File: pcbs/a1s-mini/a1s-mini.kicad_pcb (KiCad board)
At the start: 2 copper layers, 58.8 x 55.7 mm, 85 parts, among them J1 UART1, J2 SJ-3524-SMT-TR-PI, J3 Audio Out, J4 UART0, J5 USB4105-GF-A, J6 USB4105-GF-A, Q3 BC818, Q4 MBT3904DW1, Q6 MBT3904DW1, U1 ESP32 A1S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

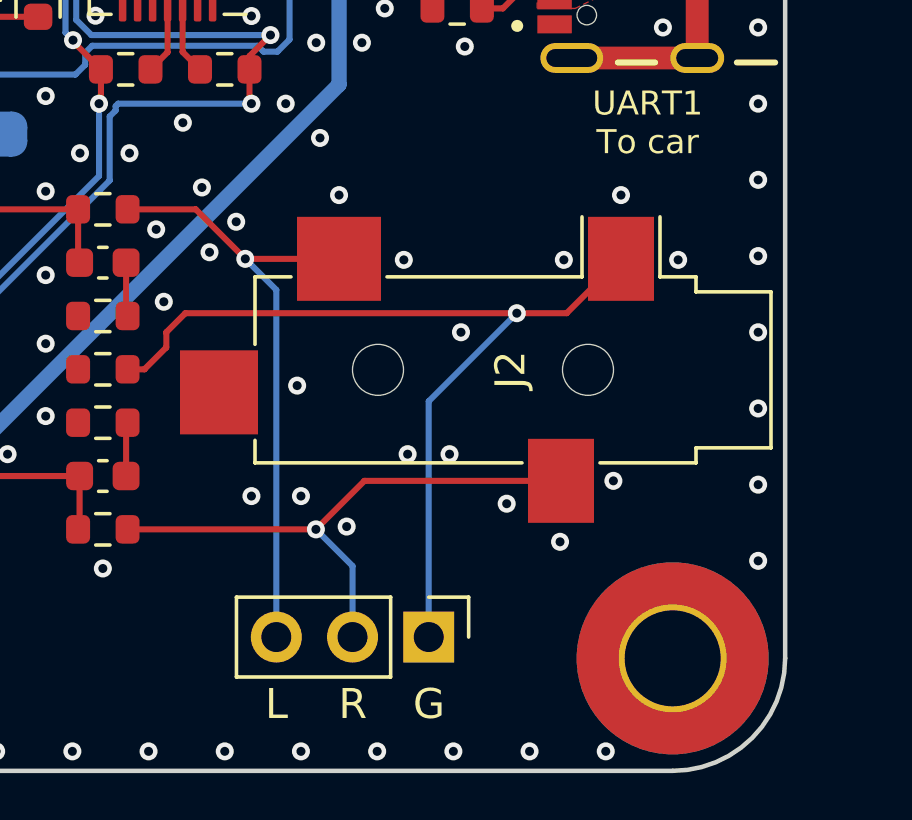
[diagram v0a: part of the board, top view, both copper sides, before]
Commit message: Moving audio jack and generating step files
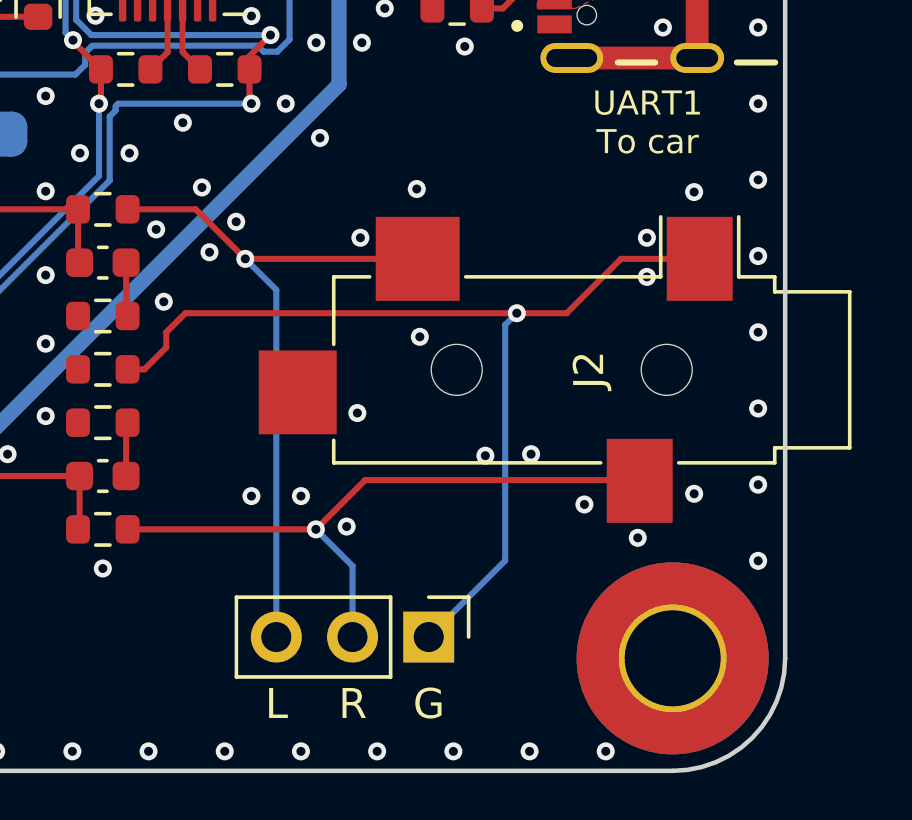
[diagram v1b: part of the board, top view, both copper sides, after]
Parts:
- moved J2 2.62 mm to (179.4, 122.8)
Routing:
- net ROUT: track 19.2 -> 21.9 mm
- net LOUT: track 20.8 -> 23.4 mm
- net AGND: track 30.3 -> 32.9 mm
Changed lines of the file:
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@@
 	(title_block
 		(title "A1S Mini Board")
-		(date "2025-03-30")
-		(rev "0.3.0")
+		(date "2025-05-25")
+		(rev "0.3.1")
 		(company "Martin Roger")
 	)
@@
 		(tags "Switch")
 		(property "Reference" "S2"
-			(at -0.85 0 270)
+			(at -0.85 0 90)
 			(layer "F.SilkS")
 			(effects
@@
 		)
 		(property "Value" "TL3305BF260QG"
-			(at -0.85 0 270)
+			(at -0.85 0 90)
 			(layer "F.SilkS")
 			(hide yes)
@@
 		)
 		(property "Datasheet" "https://configured-product-images.s3.amazonaws.com/2D/specs/TL3305BF260QG.pdf"
-			(at 0 0 270)
+			(at 0 0 90)
 			(layer "F.Fab")
 			(hide yes)
@@
 		)
 		(property "Description" "TACT, 50mA, 12VDC SPST-NO, Off-(On) Surface Mount"
-			(at 0 0 270)
+			(at 0 0 90)
 			(layer "F.Fab")
 			(hide yes)
@@
 		)
 		(embedded_fonts no)
+		(model "${PRIVATE_3DMODELS}/TL3305BF260QG.stp"
+			(offset
+				(xyz 0 0 0)
+			)
+			(scale
+				(xyz 1 1 1)
+			)
+			(rotate
+				(xyz 0 0 0)
+			)
+		)
 	)
 	(footprint "Capacitor_SMD:C_0805_2012Metric"
@@
 	(footprint "Connector_Audio:Jack_3.5mm_CUI_SJ-3524-SMT_Horizontal"
 		(layer "F.Cu")
-		(at 176.74 122.792 -90)
+		(at 179.364 122.792 -90)
 		(descr "3.5 mm, Stereo, Right Angle, Surface Mount (SMT), Audio Jack Connector (https://www.cui.com/product/resource/sj-352x-smt-series.pdf)")
 		(tags "3.5mm audio cui horizontal jack stereo")
@@
 		)
 		(embedded_fonts no)
-		(model "${KICAD6_3DMODEL_DIR}/Connector_Audio.3dshapes/Jack_3.5mm_CUI_SJ-3524-SMT_Horizontal.wrl"
+		(model "${PRIVATE_3DMODELS}/SJ-3524-SMT-TR-PI.stp"
 			(offset
-				(xyz 0 0 0)
+				(xyz 0 6 2.5)
 			)
 			(scale
@@
 			)
 			(rotate
-				(xyz 0 0 0)
+				(xyz 90 180 -0)
 			)
 		)
@@
 		(tags "Switch")
 		(property "Reference" "S1"
-			(at -0.85 0 270)
+			(at -0.85 0 90)
 			(layer "F.SilkS")
 			(effects
@@
 		)
 		(property "Value" "TL3305BF260QG"
-			(at -0.85 0 270)
+			(at -0.85 0 90)
 			(layer "F.SilkS")
 			(hide yes)
@@
 		)
 		(property "Datasheet" "https://configured-product-images.s3.amazonaws.com/2D/specs/TL3305BF260QG.pdf"
-			(at 0 0 270)
+			(at 0 0 90)
 			(layer "F.Fab")
 			(hide yes)
@@
 		)
 		(property "Description" "TACT, 50mA, 12VDC SPST-NO, Off-(On) Surface Mount"
-			(at 0 0 270)
+			(at 0 0 90)
 			(layer "F.Fab")
 			(hide yes)
@@
 		)
 		(embedded_fonts no)
+		(model "${PRIVATE_3DMODELS}/TL3305BF260QG.stp"
+			(offset
+				(xyz 0 0 0)
+			)
+			(scale
+				(xyz 1 1 1)
+			)
+			(rotate
+				(xyz 0 0 0)
+			)
+		)
 	)
 	(footprint "Resistor_SMD:R_0603_1608Metric"
@@
 	)
 	(via
-		(at 173.228 125.603)
+		(at 175.8188 125.6538)
 		(size 0.6)
 		(drill 0.3)
@@
 	)
 	(via
-		(at 182.245 119.126)
+		(at 182.7784 116.8654)
 		(size 0.6)
 		(drill 0.3)
@@
 	)
 	(via
-		(at 169.545 123.317)
+		(at 171.5516 124.2314)
 		(size 0.6)
 		(drill 0.3)
@@
 	)
 	(via
-		(at 178.308 128.524)
+		(at 180.8988 128.392002)
 		(size 0.6)
 		(drill 0.3)
@@
 	)
 	(via
-		(at 176.53 127.254)
+		(at 179.1208 127.2794)
 		(size 0.6)
 		(drill 0.3)
@@
 	)
 	(via
-		(at 180.34 116.967)
+		(at 181.2036 119.6936)
 		(size 0.6)
 		(drill 0.3)
@@
 	)
 	(via
-		(at 180.086 126.492)
+		(at 182.7784 126.9238)
 		(size 0.6)
 		(drill 0.3)
@@
 	)
 	(via
-		(at 170.942 116.967)
+		(at 171.6532 118.3894)
 		(size 0.6)
 		(drill 0.3)
@@
 	)
 	(via
-		(at 174.625 125.603)
+		(at 177.3428 125.603)
 		(size 0.6)
 		(drill 0.3)
@@
 	)
 	(via
-		(at 175.006 121.539)
+		(at 173.6344 121.6914)
 		(size 0.6)
 		(drill 0.3)
@@
 	)
 	(via
-		(at 178.435 119.126)
+		(at 181.2036 118.3894)
 		(size 0.6)
 		(drill 0.3)
@@
 	)
 	(via
-		(at 173.101 119.126)
+		(at 173.5328 116.7638)
 		(size 0.6)
 		(drill 0.3)
@@
 	)
 	(segment
-		(start 171.787 126.492)
-		(end 178.34 126.492)
+		(start 170.17 128.109)
+		(end 171.8124 126.4666)
 		(width 0.2032)
 		(layer "F.Cu")
@@
 	)
 	(segment
-		(start 170.17 128.109)
-		(end 171.787 126.492)
+		(start 180.9386 126.4666)
+		(end 180.964 126.492)
+		(width 0.2032)
+		(layer "F.Cu")
+		(net 33)
+	)
+	(segment
+		(start 171.8124 126.4666)
+		(end 180.9386 126.4666)
 		(width 0.2032)
 		(layer "F.Cu")
@@
 	)
 	(segment
-		(start 178.528 120.904)
-		(end 180.34 119.092)
+		(start 163.893 122.775)
+		(end 164.455 122.775)
 		(width 0.2032)
 		(layer "F.Cu")
@@
 	)
 	(segment
-		(start 163.893 122.775)
-		(end 164.455 122.775)
+		(start 180.34 119.092)
+		(end 182.964 119.092)
 		(width 0.2032)
 		(layer "F.Cu")
@@
 		(net 34)
 	)
+	(segment
+		(start 178.528 120.904)
+		(end 180.34 119.092)
+		(width 0.2032)
+		(layer "F.Cu")
+		(net 34)
+	)
 	(via
 		(at 176.867 120.904)
@@
 	)
 	(segment
-		(start 173.931 123.84)
+		(start 176.4792 121.2918)
 		(end 176.867 120.904)
 		(width 0.2032)
@@
 	(segment
 		(start 173.931 131.699)
-		(end 173.931 123.84)
+		(end 176.4792 129.1508)
+		(width 0.2032)
+		(layer "B.Cu")
+		(net 34)
+	)
+	(segment
+		(start 176.4792 129.1508)
+		(end 176.4792 121.2918)
 		(width 0.2032)
 		(layer "B.Cu")
@@
 	)
 	(segment
-		(start 167.816 119.092)
-		(end 170.94 119.092)
+		(start 163.893 117.441)
+		(end 166.165 117.441)
 		(width 0.2032)
 		(layer "F.Cu")
@@
 	)
 	(segment
-		(start 163.893 117.441)
-		(end 166.165 117.441)
+		(start 167.816 119.092)
+		(end 173.564 119.092)
 		(width 0.2032)
 		(layer "F.Cu")
@@
 	(group ""
 		(members "010ed563-2973-4e7b-880b-ac3cfb64729f" "01276b8d-2b07-49d3-8b35-fdecf44a092f"
-			"019a97af-5de7-4efe-972a-8204659258c9" "0bc8b6e9-098f-455f-a2b6-f17a9d852d70"
-			"0be3b034-8138-41b2-8697-4d37a17a84a4" "1277cde9-51e9-4f09-85db-96225ab56807"
+			"0bc8b6e9-098f-455f-a2b6-f17a9d852d70" "0be3b034-8138-41b2-8697-4d37a17a84a4"
+			"1277cde9-51e9-4f09-85db-96225ab56807" "16802a33-bfa3-482c-9e4f-84b36f7dd177"
 			"1f55c12f-7500-44a8-9a40-de71dd5c2e10" "2320cddf-c750-480e-808d-3dbd92fe251d"
 			"2635c3ab-f4d5-4ea3-8317-cc488b28a56d" "27dbc821-cc4b-4ea6-ad66-3b0d750dda18"
 			"2ce1c9cf-3d4a-4b50-9b31-e205f036385f" "304ad4f1-862e-4027-8de5-301e5c9bb41e"
-			"3283374a-ec22-4d03-80e8-8ad2329dba5f" "355cc9c1-65e6-4e68-a974-cbbdd1257902"
-			"35b4e900-2bed-4ea8-b7e7-b8250b1e7e7e" "3bdbe9e9-9197-4c0e-a543-8e46b804b0dc"
-			"4782a773-90a6-4148-b0a7-9dd6eefd5aad" "4c52461a-149b-4eec-a428-97cf9bf35de8"
-			"5c99fa24-4401-4d5a-997f-6d78716bc5f5" "5d014071-d2dc-4647-beaf-cba16b22cd9f"
-			"8ee44f09-00b1-4cb8-a334-ebd31d421489" "9464d84d-46a6-4a53-afc5-3f068152bc37"
-			"b62076f0-405c-4baa-b1f5-f8bcf2d20abd" "b8b7875e-48a3-4bdb-b0db-3715a3c873ef"
-			"bbbde7ee-d092-4d43-b47f-1ea3ba58ced9" "bce551e3-f423-4053-9973-22389445b177"
-			"c368fc1b-c9c4-44e1-99a4-be5dbafa2c78" "c8101ae0-b9df-476c-a6fa-1832a03521fa"
-			"cd4b371d-78d5-4685-ade5-c527481dbb93" "cea4292e-6d22-40c0-a3ef-10f58e66caf0"
-			"da937504-e6c3-46ed-a387-d5830cbeae16" "e6eb6426-162a-4115-b2a7-4587bebc7a9c"
-			"ec039ec8-b2e6-4db4-9b6e-e6335db5a8b9" "eef33f5e-9a19-4485-b453-f566f85e2875"
-			"f202a222-b79e-45f9-99d0-3975618f77dc" "f317a6f2-5063-4160-a05b-54ee9751d1aa"
-			"f3bd3b37-f068-4793-a604-252e1f766a4c"
+			"3bdbe9e9-9197-4c0e-a543-8e46b804b0dc" "4782a773-90a6-4148-b0a7-9dd6eefd5aad"
+			"4c52461a-149b-4eec-a428-97cf9bf35de8" "5c99fa24-4401-4d5a-997f-6d78716bc5f5"
+			"5d014071-d2dc-4647-beaf-cba16b22cd9f" "6428761d-30dd-4c5b-ad00-7d5e50292759"
+			"6544f0f1-11bd-4078-b5a1-d2c90a1d2fdb" "6767676a-2073-418f-8eb7-74b574d95305"
+			"85cc0403-8287-4ccc-9240-b6bb848303b7" "8ee44f09-00b1-4cb8-a334-ebd31d421489"
+			"9464d84d-46a6-4a53-afc5-3f068152bc37" "98181832-dbcc-4c7b-bd6b-59713328d394"
+			"a62cc70d-f242-49f9-aa8d-1462106ee1b0" "b62076f0-405c-4baa-b1f5-f8bcf2d20abd"
+			"b78e9ece-bcde-4c88-a0b1-0686802ee165" "b8b7875e-48a3-4bdb-b0db-3715a3c873ef"
+			"bbbde7ee-d092-4d43-b47f-1ea3ba58ced9" "c368fc1b-c9c4-44e1-99a4-be5dbafa2c78"
+			"c8101ae0-b9df-476c-a6fa-1832a03521fa" "cd4b371d-78d5-4685-ade5-c527481dbb93"
+			"cea4292e-6d22-40c0-a3ef-10f58e66caf0" "da937504-e6c3-46ed-a387-d5830cbeae16"
+			"e6eb6426-162a-4115-b2a7-4587bebc7a9c" "ec039ec8-b2e6-4db4-9b6e-e6335db5a8b9"
+			"f2edf953-51db-454e-9f92-fcd6f25702e4" "f317a6f2-5063-4160-a05b-54ee9751d1aa"
+			"f3bd3b37-f068-4793-a604-252e1f766a4c" "f6861546-4d09-4eba-b4d5-1c9548f0ff14"
 		)
 	)

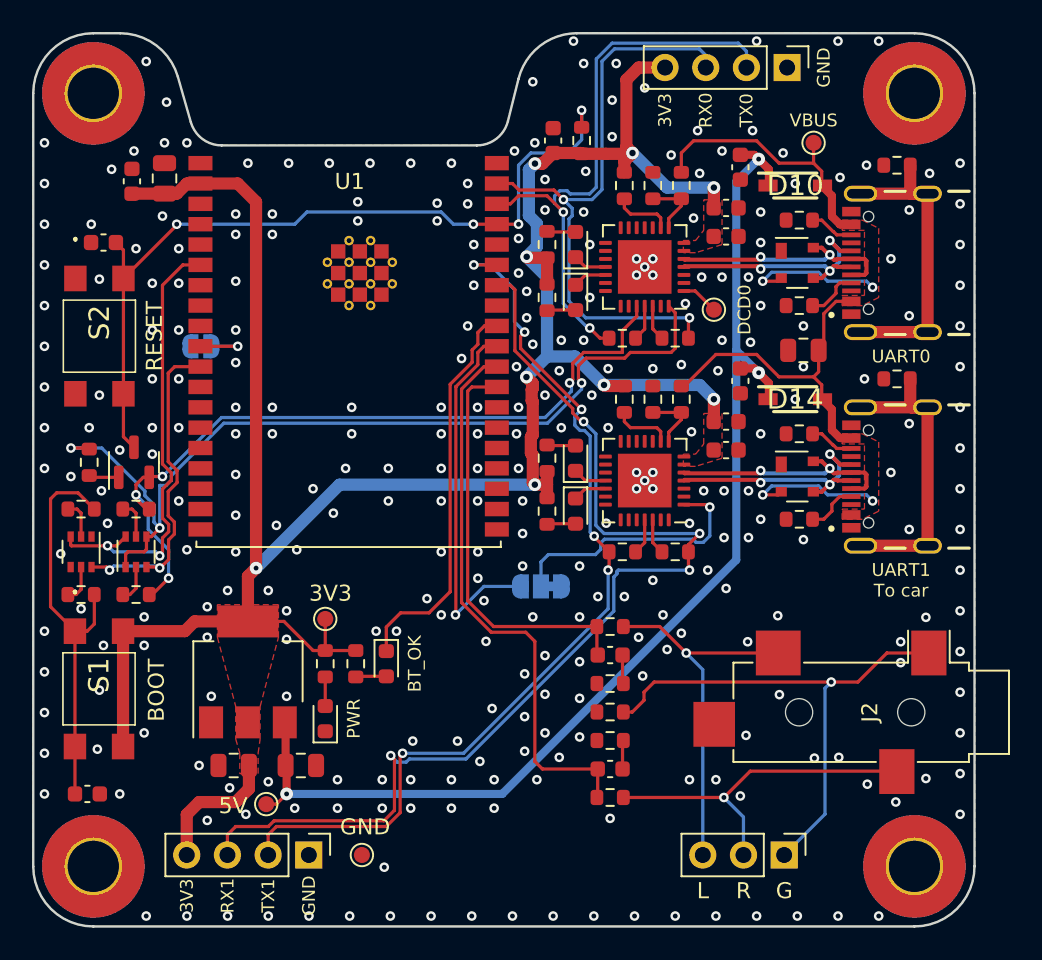
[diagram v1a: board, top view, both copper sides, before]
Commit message: Move to CP2102 non N
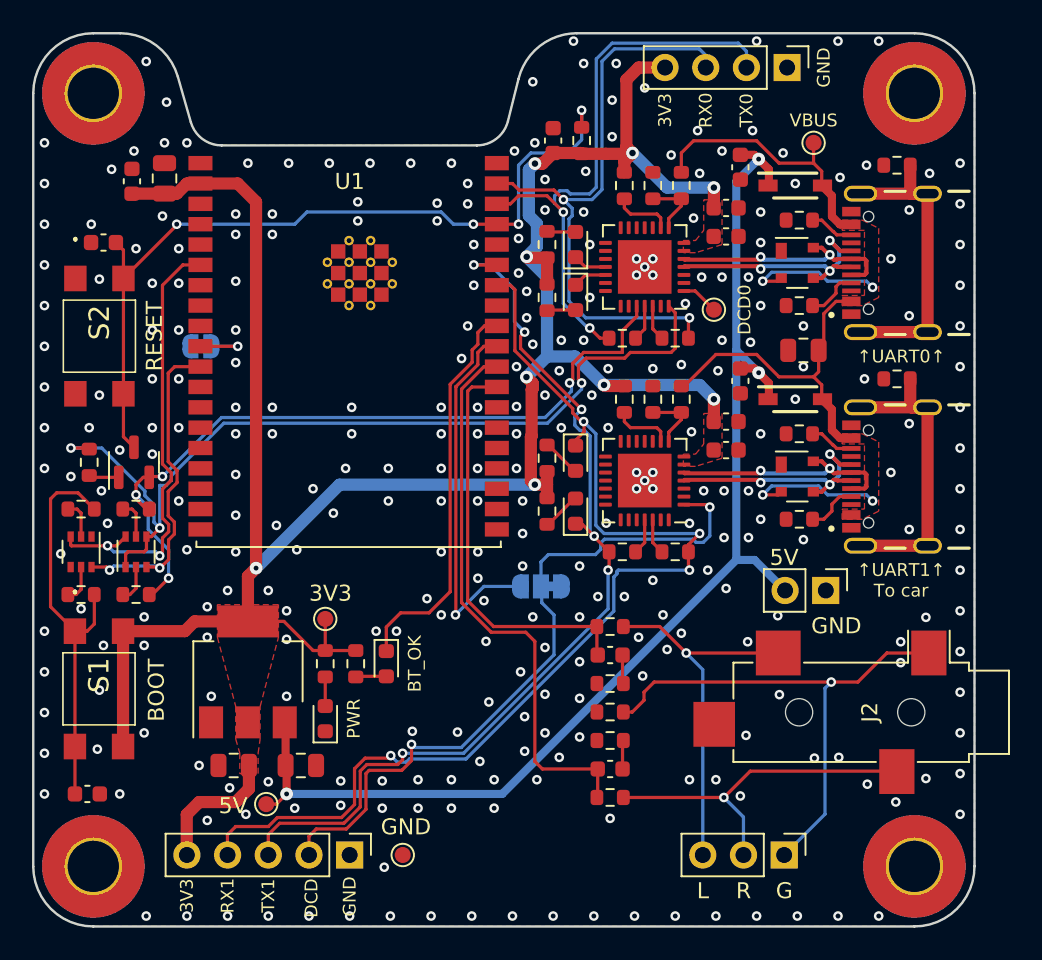
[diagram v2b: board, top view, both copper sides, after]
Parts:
- added J7: 5V, Connector_PinHeader_2.54mm:PinHeader_1x02_P2.54mm_Vertical, F.Cu at (176.5, 115.2)
- J1: footprint Connector_PinHeader_2.54mm:PinHeader_1x04_P2.54mm_Vertical -> Connector_PinHeader_2.54mm:PinHeader_1x05_P2.54mm_Vertical
- U4: value CP2102N -> CP2102-GM
- moved R35 3.30 mm to (159.1, 110.2), turned to -90 degrees
- moved D11 3.30 mm to (160.9, 110.2)
- moved D9 3.30 mm to (160.9, 106.9)
- moved R34 3.30 mm to (159.1, 106.9), turned to 90 degrees
- moved J1 2.55 mm to (146.8, 131.7)
- moved GND1 2.55 mm to (150.1, 131.7)
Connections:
- net /CP2102_0/CTS renamed /CP2102N_0/CTS
- net /CP2102_0/D+ renamed /CP2102N_0/D+
- net /CP2102_0/D- renamed /CP2102N_0/D-
- net /CP2102_0/DCD renamed /CP2102N_0/DCD
- net /CP2102_0/DSR renamed /CP2102N_0/DSR
- net /CP2102_0/RI renamed /CP2102N_0/RI
- D11 pad 1: Net-(D11-K) -> TXD1
- D9 pad 1: Net-(D9-K) -> RXD1
- J1 pad 2: TXD1 -> /CP2102_1/DCD
- J1 pad 3: RXD1 -> TXD1
- J1 pad 4: +3.3V -> RXD1
- U4 pad 18: Net-(D11-K) -> unconnected-(U4-~{RXT}/GPIO.1-Pad18)
- U4 pad 19: Net-(D9-K) -> unconnected-(U4-~{TXT}/GPIO.0-Pad19)
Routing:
- net /CP2102_1/DCD: track 16.6 -> 44.4 mm, vias 1 -> 2
- net +5V: track 74.1 -> 77.9 mm
- net Net-(D9-K): track 2.12 -> 0.00 mm
- net Net-(D11-K): track 2.12 -> 0.00 mm
- net TXD1: track 58.2 -> 59.1 mm
- net RXD1: track 68.4 -> 69.1 mm
- net Net-(D11-A): track 1.79 -> 2.45 mm
- net Net-(D9-A): track 1.79 -> 2.45 mm
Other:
- board text added: "↑UART0↑"
- board text added: "↑UART1↑ To car"
- board text removed: "UART0"
- board text removed: "UART1 To car"

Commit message: Collateral update of A1S mini (TX LEDs fix)
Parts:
- moved D1 3.30 mm to (160.9, 93.6)
- moved D2 3.30 mm to (160.9, 96.9)
- moved R1 3.30 mm to (159.1, 93.6), turned to 90 degrees
- moved R2 3.30 mm to (159.1, 96.9), turned to -90 degrees
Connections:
- D1 pad 1: Net-(D1-K) -> RXD0
- D2 pad 1: Net-(D2-K) -> TXD0
- U3 pad 18: Net-(D2-K) -> unconnected-(U3-~{RXT}/GPIO.1-Pad18)
- U3 pad 19: Net-(D1-K) -> unconnected-(U3-~{TXT}/GPIO.0-Pad19)
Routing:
- net RXD0: track 38.9 -> 41.2 mm
- net Net-(D1-K): track 2.12 -> 0.00 mm
- net Net-(D2-K): track 2.12 -> 0.00 mm
- net TXD0: track 37.5 -> 39.0 mm
- net Net-(D2-A): track 1.79 -> 2.45 mm
- net Net-(D1-A): track 1.79 -> 2.45 mm

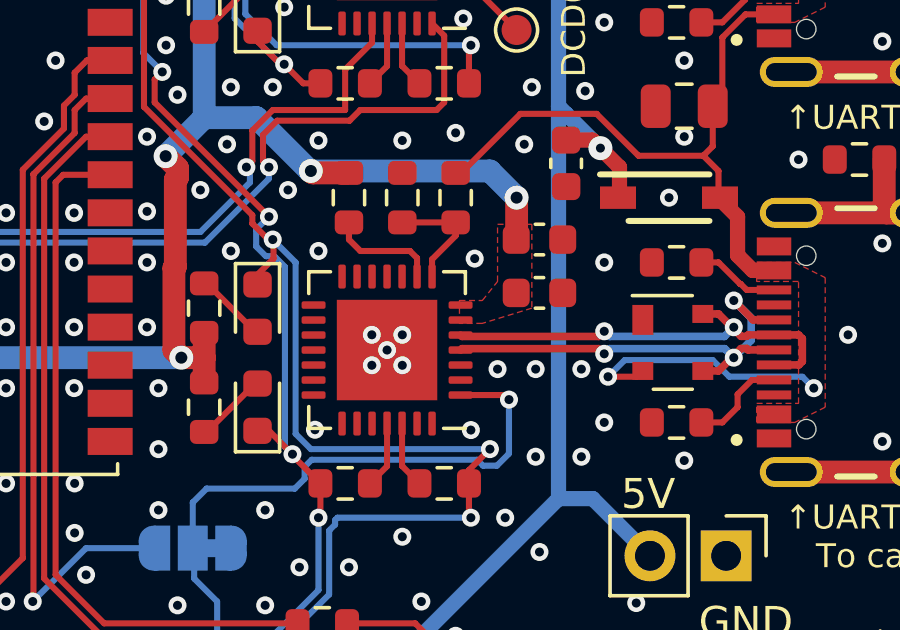
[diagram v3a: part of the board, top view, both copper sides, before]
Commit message: A1S updated to CP2104
Version numbers also updated
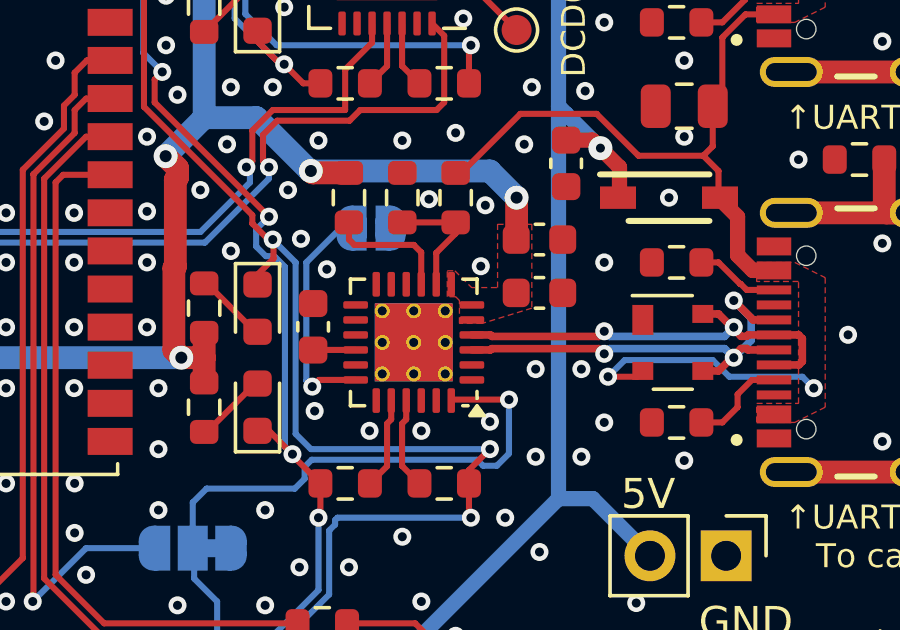
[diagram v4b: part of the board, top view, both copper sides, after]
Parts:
- removed U4: CP2102-GM, Package_DFN_QFN:QFN-28-1EP_5x5mm_P0.5mm_EP3.35x3.35mm
- added C19: 4.7uF 16V, Capacitor_SMD:C_0603_1608Metric, F.Cu at (162.8, 107.6)
- added JP3: CTS1, Jumper:SolderJumper-2_P1.3mm_Open_RoundedPad1.0x1.5mm, B.Cu at (164.7, 104.3)
- added U6: CP2104, Package_DFN_QFN:QFN-24-1EP_4x4mm_P0.5mm_EP2.6x2.6mm_ThermalVias, F.Cu at (166.1, 108.1)
- R23: value 22.1K 1% -> 24K 1%
- R24: value 47.5K 1% -> 47K 1%
- U3: value CP2102N -> CP2102-GM
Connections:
- net /CP2102_1/D+ renamed /CP2104/D+
- net /CP2102_1/D- renamed /CP2104/D-
- net /CP2102_1/DCD renamed /CP2104/DCD
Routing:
- net /CP2104/CTS: track 0.00 -> 7.74 mm, vias 0 -> 1
- net Net-(U6-VPP): track 0.00 -> 1.42 mm
- net Net-(U6-TXD): track 2.24 -> 3.06 mm
- net Net-(U6-RXD): track 2.23 -> 3.06 mm
- net Net-(U6-~{RST}): track 3.71 -> 4.22 mm
- net GND: vias 304 -> 303
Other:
- board text added: "CTS"
